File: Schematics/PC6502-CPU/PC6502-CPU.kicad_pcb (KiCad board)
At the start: 4 copper layers, 100 x 100 mm, 79 parts, among them J1 BUS, J2 Conn_01x02, J3 USB_C_Receptacle_USB2.0_16P, J4 TEST, J5 Conn_02x05_Odd_Even, J6 Conn_02x02_Odd_Even, Q1 IRLML6402, U2 AS6C4008-55PCN, U3 SST39SF010, U4 ATF1502AS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

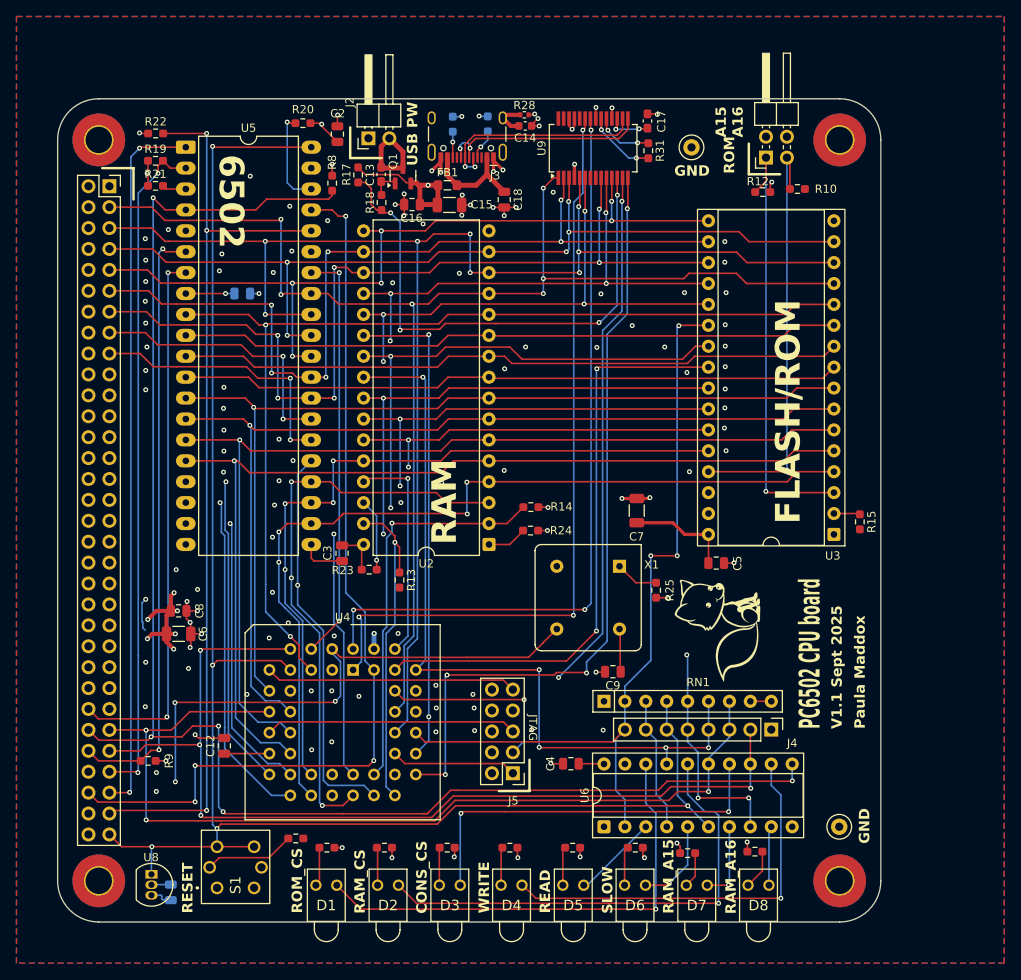
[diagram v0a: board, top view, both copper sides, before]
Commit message: Updated following testing
New CPLD code for CPU and VIA
Fixed mistakes with CPU Board and upped to Rev 1.2 (My Rev 1.1 has mods on)
Updated README
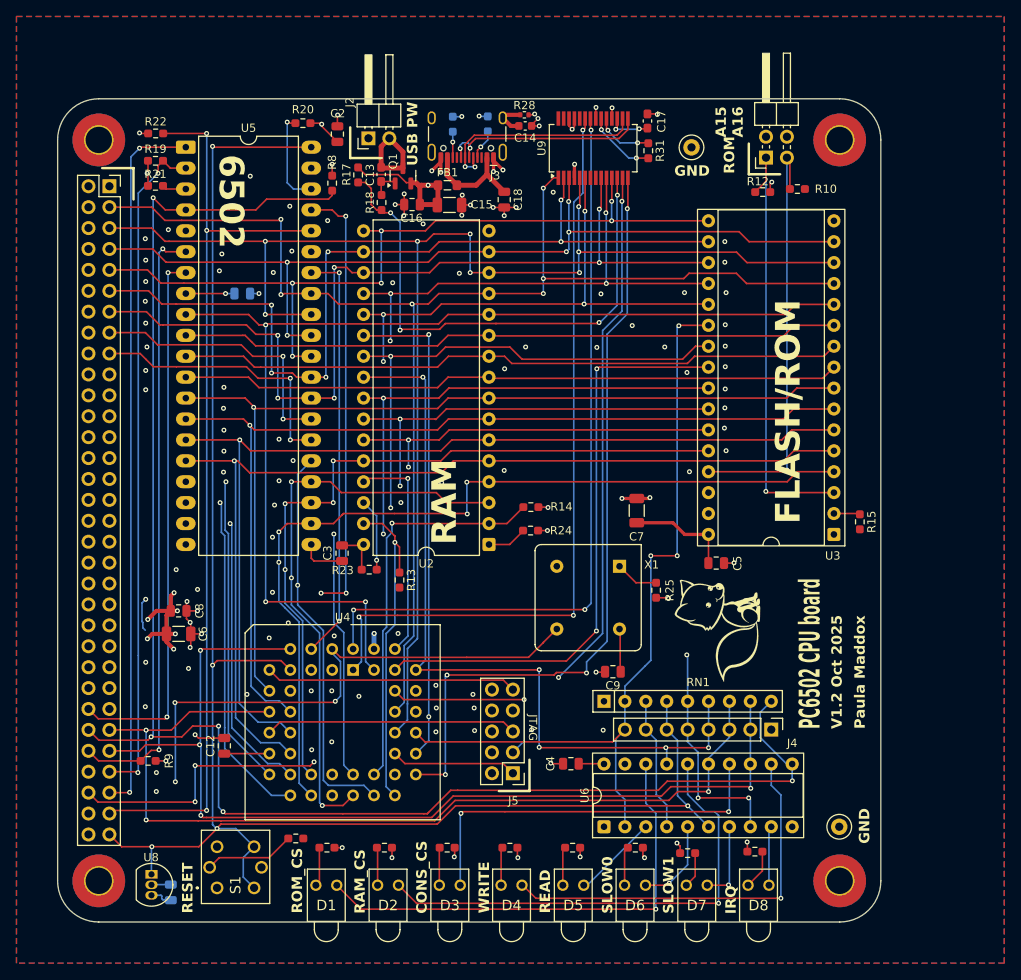
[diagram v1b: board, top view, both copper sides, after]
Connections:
- RN1 pad 8: GND -> nSLOW1
- RN1 pad 9: GND -> nIRQ
- S1 pad 2: nRES -> GND
- S1 pad 3: GND -> nRES
- U4 pad 43: CPU_CLK -> /A0
- U4 pad 5: /A0 -> CPU_CLK
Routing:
- net /A0: track 136.8 -> 147.0 mm, vias 2 -> 3
- net nIRQ: track 189.9 -> 200.0 mm
- net nRES: track 204.4 -> 210.1 mm
- net CPU_CLK: track 111.9 -> 107.5 mm, vias 4 -> 6
- net nSLOW1: track 118.1 -> 121.5 mm
- net GND: track 72.8 -> 70.3 mm
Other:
- board text added: "IRQ"
- board text added: "SLOW0"
- board text added: "SLOW1"
- board text added: "V1.2 Oct 2025"
- board text removed: "RAM_A15"
- board text removed: "RAM_A16"
- board text removed: "SLOW"
- board text removed: "V1.1 Sept 2025"

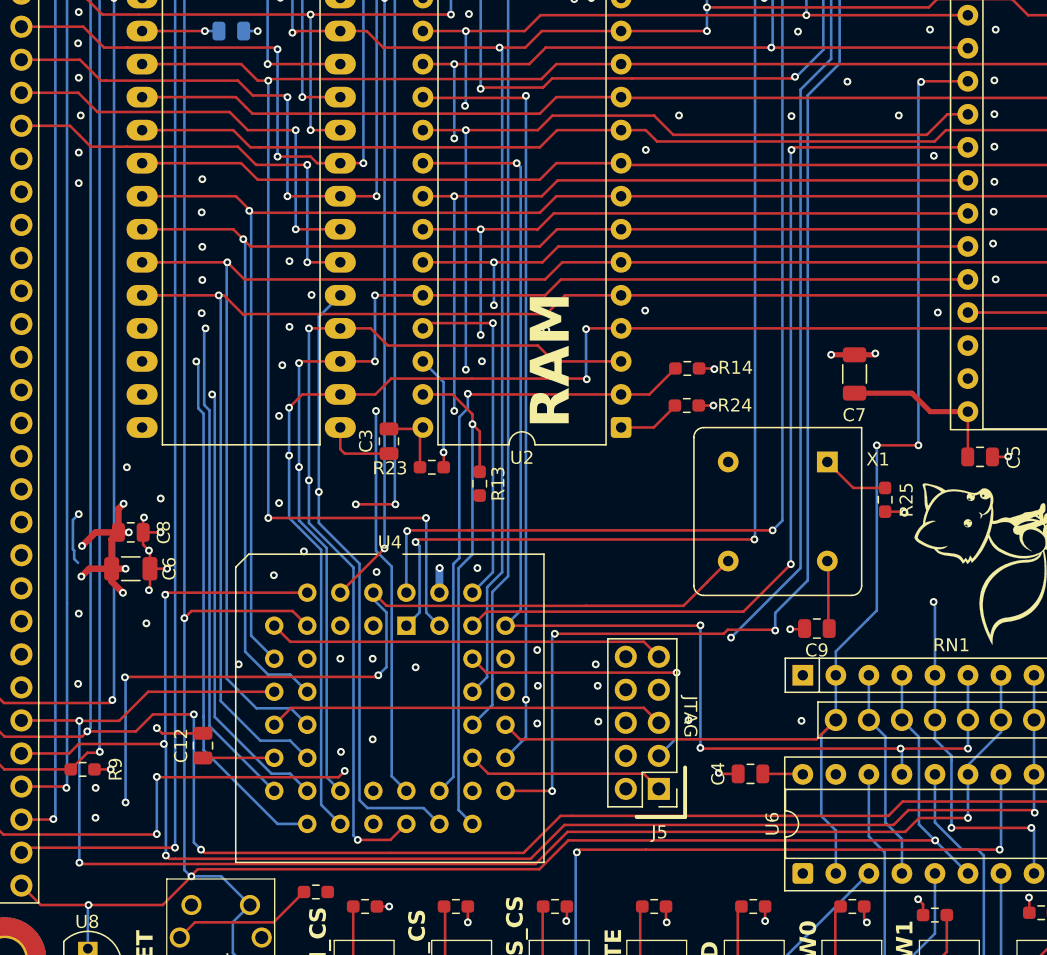
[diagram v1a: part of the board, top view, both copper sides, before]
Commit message: Updated Schematics and CPLD files
Files updated for the CPU & FM Speech board
Also revised CPLDs for CPU, VIA and Compact Flasg
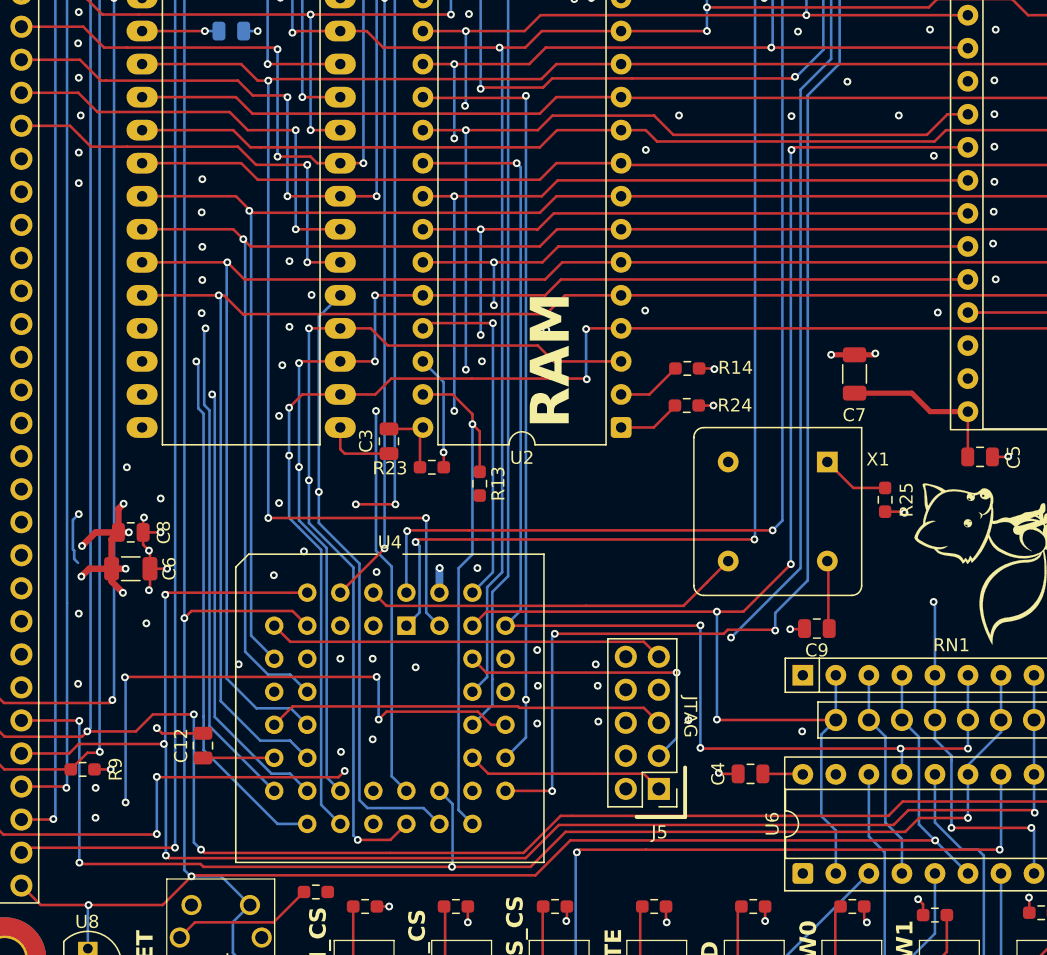
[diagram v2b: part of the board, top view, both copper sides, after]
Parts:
- U4: value ATF1502AS -> ATF1504AS
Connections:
- J4 pad 8: nROM_CS -> ROM_nR
- R14 pad 1: RAM_A16 -> Net-(U2-A16)
- RN1 pad 2: nROM_CS -> ROM_nR
- U2 pad 2: RAM_A16 -> Net-(U2-A16)
- U3 pad 22: nROM_CS -> GND
- U4 pad 11: nSLOW0 -> unconnected-(U4-I/O/PD1-Pad11)
- U4 pad 2: SYSCLK -> CLK_x2
- U4 pad 27: RAM_A16 -> nSLOW0
- U4 pad 33: nROM_CS -> SYSCLK
- U6 pad 2: nROM_CS -> ROM_nR
- X1 pad 5: SYSCLK -> CLK_x2
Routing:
- net nROM_CS: track 96.5 -> 0.00 mm, vias 3 -> 0
- net RAM_A16: track 48.2 -> 0.00 mm, vias 1 -> 0
- net ROM_nR: track 72.0 -> 105.6 mm, vias 2 -> 4
- net CLK_x2: track 0.00 -> 29.1 mm
- net SYSCLK: track 76.4 -> 53.8 mm, vias 3 -> 4
- net nSLOW0: track 113.1 -> 103.6 mm, vias 3 -> 4
- net Net-(U2-A16): track 0.00 -> 5.00 mm

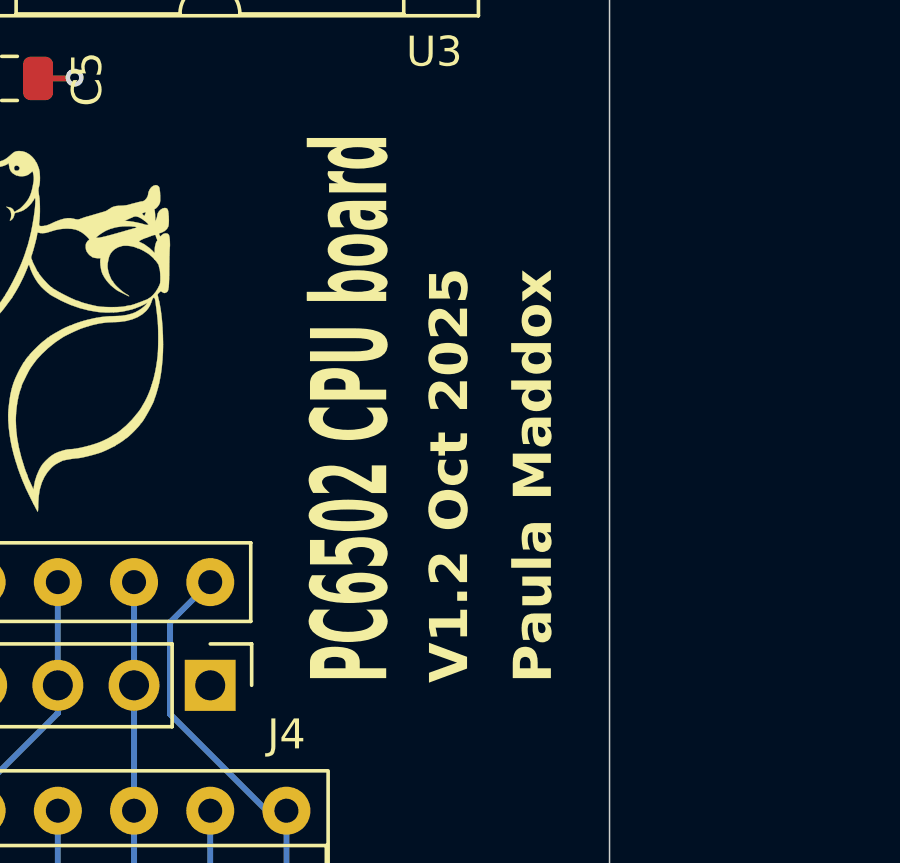
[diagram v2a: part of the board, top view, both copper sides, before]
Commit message: Updated silk screen
Updated silk screen on CPU board to V1.3
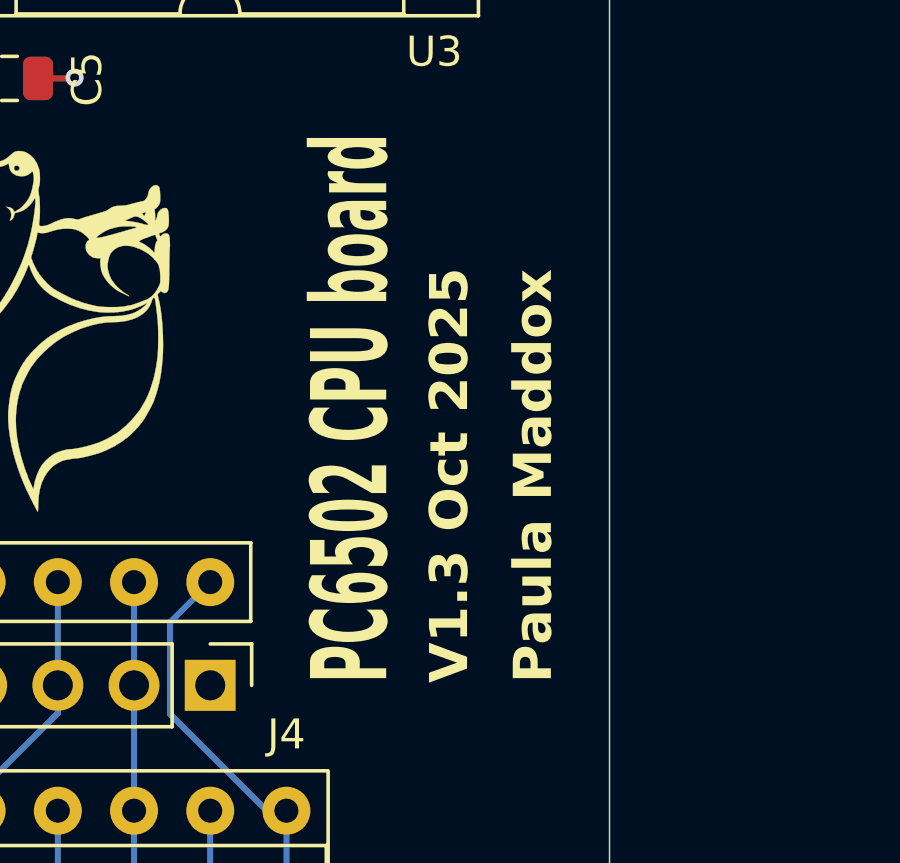
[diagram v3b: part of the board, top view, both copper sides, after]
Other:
- board text added: "V1.3 Oct 2025"
- board text removed: "V1.2 Oct 2025"
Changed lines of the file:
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@@
 		)
 	)
-	(gr_text "V1.2 Oct 2025"
+	(gr_text "V1.3 Oct 2025"
 		(at 195.406 126.55 90)
 		(layer "F.SilkS")
